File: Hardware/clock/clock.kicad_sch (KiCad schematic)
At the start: 19 parts, among them J1 Barrel_Jack_Switch, U1 WEMOS_C3_mini, U2 MAX7221xNG, U3 SBC18-11EGWA, U4 LM2596S-5, U5 SBC18-11EGWA, U6 SBC18-11EGWA, U7 SBC18-11EGWA

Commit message: Refactor code structure for improved readability and maintainability
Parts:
- removed C3: 104, Capacitor_THT:C_Disc_D3.0mm_W1.6mm_P2.50mm, symbol SparkFun-Capacitor:C
- removed D1: M7, PCM_JLCPCB:D_SMA, symbol PCM_JLCPCB-Diodes:General,M7
- removed R1: 10k, Resistor_THT:R_Axial_DIN0204_L3.6mm_D1.6mm_P5.08mm_Horizontal, symbol Device:R
- removed U1: WEMOS_C3_mini, RF_Module:WEMOS_C3_mini, symbol RF_Module:WEMOS_C3_mini
- added C1: 10uF, Capacitor_SMD:CP_Elec_4x5.4, symbol SparkFun-Capacitor:C
- added C10, C11, C12, C2, C6, C8: 100nF, SparkFun-Capacitor:C_0805_2012Metric, symbol SparkFun-Capacitor:C
- added C7: 22uF, Capacitor_SMD:C_0805_2012Metric_Pad1.18x1.45mm_HandSolder, symbol SparkFun-Capacitor:C
- added D3: SS34, Diode_SMD:D_SMA, symbol Diode:SS34
- added J2: Conn_02x03_Top_Bottom, Connector_IDC:IDC-Header_2x03_P2.54mm_Horizontal, symbol Connector_Generic:Conn_02x03_Top_Bottom
- added Q1, Q2: BC817, Package_TO_SOT_SMD:SOT-23, symbol Transistor_BJT:BC817
- added R1, R2, R3, R4: 10kΩ, PCM_JLCPCB:R_0805, symbol PCM_JLCPCB-Resistors:0805,10kΩ
- added SW1: PTH_RA_h7.5mm, SparkFun-Switch:Push_PTH_RA_8-020_h7.5mm, symbol SparkFun-Switch:SPST_Push_PTH_RA_h7.5mm
- added U4: ESP32-WROOM-32, RF_Module:ESP32-WROOM-32, symbol RF_Module:ESP32-WROOM-32
- added U7: AMS1117-3.3, Package_TO_SOT_SMD:SOT-223-3_TabPin2, symbol Regulator_Linear:AMS1117-3.3
- C3: renamed from C1; footprint Capacitor_THT:C_Radial_D8.0mm_H11.5mm_P3.50mm -> Capacitor_THT:C_Radial_D6.3mm_H7.0mm_P2.50mm
- C4: value 1uF -> 100nF; footprint Capacitor_THT:C_Radial_D4.0mm_H5.0mm_P1.50mm -> SparkFun-Capacitor:C_0805_2012Metric
- C5: value 104 -> 22uF; footprint Capacitor_THT:C_Disc_D3.0mm_W1.6mm_P2.50mm -> SparkFun-Fuse:1206
- D1: renamed from D3; footprint SparkFun-LED:LED_0603_1608Metric_Red -> LED_THT:LED_D3.0mm
- D2: renamed from D4; footprint SparkFun-LED:LED_0603_1608Metric_Red -> LED_THT:LED_D3.0mm
- renumbered C2 to C9, D2 to D4, U3 to U1, U5 to U2, U6 to U3, U7 to U5, U2 to U6, U4 to U8
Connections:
- net +5V: now also C1.1, C10.1, C12.1, C2.1, J2.3 (Pin_3), R1.2, U7.3 (VI); no longer C4.1, C5.1
- net GND: now also C1.2, C10.2, C11.2, C12.2, C2.2, C6.2, C7.2, C8.2, J2.6 (Pin_6), SW1.1, U4.1 (GND), U4.15 (GND), U4.38 (GND), U4.39 (GND), U7.1 (GND)
- net pwr_in: now also C4.1, D3.1 (K)
- net at J1.1: now also D3.2 (A)
- net at U6.18 (ISET): now also R1.1
- net MOSI: now reaches U6.1 (DIN)
- net MOSI: now also U4.37 (IO23)
- net CS: now reaches U6.12 (~{CS})
- net CS: now also U4.29 (IO5)
- net CLK: now reaches U6.13 (CLK)
- net CLK: now also U4.30 (IO18)
- new net: Q1.1 (B), R3.2
- new net: Q2.1 (B), R2.2
- new net 3.3V: C5.1, C6.1, C7.1, C8.1, R4.2, U4.2 (VDD), U7.2 (VO)
- new net DTR: J2.1 (Pin_1), Q2.2 (E), R3.1
- new net EN: C11.1, Q1.3 (C), R4.1, SW1.2, U4.3 (EN)
- new net IO0: Q2.3 (C), U4.25 (IO0)
- new net RTS: J2.4 (Pin_4), Q1.2 (E), R2.1
- new net RXD0: J2.2 (Pin_2), U4.34 (RXD0/IO3)
- new net TXD0: J2.5 (Pin_5), U4.35 (TXD0/IO1)
- no-connect marks 0 -> 8
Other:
- moved on the sheet: C3, C9, D4, J1, L1, U8

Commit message: Refactor code structure for improved readability and maintainability
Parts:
- removed J2: Conn_02x03_Top_Bottom, Connector_IDC:IDC-Header_2x03_P2.54mm_Horizontal, symbol Connector_Generic:Conn_02x03_Top_Bottom
- added J3: Conn_02x03_Odd_Even, Connector_IDC:IDC-Header_2x03_P2.54mm_Horizontal, symbol Connector_Generic:Conn_02x03_Odd_Even
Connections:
- net +5V: now also J3.5 (Pin_5)
- net DTR: now also J3.1 (Pin_1)
- net GND: now also J3.6 (Pin_6)
- net RTS: now also J3.2 (Pin_2)
- net RXD0: now also J3.3 (Pin_3)
- net TXD0: now also J3.4 (Pin_4)
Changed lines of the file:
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@@
 	(wire
 		(pts
+			(xy 101.6 138.43) (xy 107.95 138.43)
+		)
+		(stroke
+			(width 0)
+			(type default)
+		)
+	)
+	(wire
+		(pts
 			(xy 21.59 163.83) (xy 26.67 163.83)
 		)
@@
 	(wire
 		(pts
-			(xy 101.6 120.65) (xy 106.68 120.65)
-		)
-		(stroke
-			(width 0)
-			(type default)
-		)
-	)
-	(wire
-		(pts
 			(xy 22.86 114.3) (xy 27.94 114.3)
 		)
@@
 	(wire
 		(pts
-			(xy 118.11 83.82) (xy 123.19 83.82)
+			(xy 46.99 87.63) (xy 46.99 90.17)
 		)
 		(stroke
@@
 	(wire
 		(pts
-			(xy 46.99 87.63) (xy 46.99 90.17)
+			(xy 22.86 111.76) (xy 27.94 111.76)
 		)
 		(stroke
@@
 	(wire
 		(pts
-			(xy 22.86 111.76) (xy 27.94 111.76)
+			(xy 116.84 86.36) (xy 123.19 86.36)
 		)
 		(stroke
@@
 	(wire
 		(pts
-			(xy 273.05 146.05) (xy 273.05 149.86)
+			(xy 101.6 148.59) (xy 107.95 148.59)
 		)
 		(stroke
@@
 	(wire
 		(pts
-			(xy 101.6 148.59) (xy 106.68 148.59)
+			(xy 273.05 146.05) (xy 273.05 149.86)
 		)
 		(stroke
@@
 	(wire
 		(pts
-			(xy 118.11 81.28) (xy 123.19 81.28)
-		)
-		(stroke
-			(width 0)
-			(type default)
-		)
-	)
-	(wire
-		(pts
 			(xy 40.64 114.3) (xy 43.18 114.3)
 		)
@@
 	(wire
 		(pts
-			(xy 243.84 147.32) (xy 243.84 146.05)
+			(xy 116.84 81.28) (xy 123.19 81.28)
 		)
 		(stroke
@@
 	(wire
 		(pts
-			(xy 44.45 118.11) (xy 44.45 116.84)
+			(xy 243.84 147.32) (xy 243.84 146.05)
 		)
 		(stroke
@@
 	(wire
 		(pts
-			(xy 17.78 59.69) (xy 20.32 59.69)
+			(xy 44.45 118.11) (xy 44.45 116.84)
 		)
 		(stroke
@@
 	(wire
 		(pts
-			(xy 143.51 60.96) (xy 147.32 60.96)
+			(xy 17.78 59.69) (xy 20.32 59.69)
 		)
 		(stroke
@@
 	(wire
 		(pts
-			(xy 255.27 146.05) (xy 261.62 146.05)
+			(xy 143.51 60.96) (xy 147.32 60.96)
 		)
 		(stroke
@@
 	(wire
 		(pts
-			(xy 57.15 96.52) (xy 57.15 99.06)
+			(xy 255.27 146.05) (xy 261.62 146.05)
 		)
 		(stroke
@@
 	(wire
 		(pts
-			(xy 118.11 86.36) (xy 123.19 86.36)
+			(xy 57.15 96.52) (xy 57.15 99.06)
 		)
 		(stroke
@@
 	(wire
 		(pts
+			(xy 116.84 83.82) (xy 123.19 83.82)
+		)
+		(stroke
+			(width 0)
+			(type default)
+		)
+	)
+	(wire
+		(pts
 			(xy 53.34 176.53) (xy 53.34 180.34)
 		)
@@
 	(wire
 		(pts
-			(xy 41.91 46.99) (xy 44.45 46.99)
+			(xy 101.6 120.65) (xy 106.68 120.65)
 		)
 		(stroke
@@
 	(wire
 		(pts
-			(xy 180.34 106.68) (xy 180.34 110.49)
+			(xy 41.91 46.99) (xy 44.45 46.99)
 		)
 		(stroke
@@
 	(wire
 		(pts
-			(xy 38.1 171.45) (xy 45.72 171.45)
+			(xy 180.34 106.68) (xy 180.34 110.49)
 		)
 		(stroke
@@
 	(wire
 		(pts
-			(xy 101.6 138.43) (xy 106.68 138.43)
+			(xy 38.1 171.45) (xy 45.72 171.45)
 		)
 		(stroke
@@
 		)
 	)
-	(label "MOSI"
-		(at 118.11 86.36 0)
+	(label "CS"
+		(at 116.84 81.28 0)
 		(effects
 			(font
@@
 		)
 	)
-	(label "CLK"
-		(at 106.68 138.43 0)
-		(effects
-			(font
-				(size 1.27 1.27)
-			)
-			(justify left bottom)
-		)
-	)
 	(label "D"
 		(at 147.32 53.34 0)
@@
 		)
 	)
-	(label "CS"
-		(at 118.11 81.28 0)
-		(effects
-			(font
-				(size 1.27 1.27)
-			)
-			(justify left bottom)
-		)
-	)
 	(label "TXD0"
 		(at 43.18 114.3 0)
@@
 		)
 	)
-	(label "MOSI"
-		(at 106.68 148.59 0)
-		(effects
-			(font
-				(size 1.27 1.27)
-			)
-			(justify left bottom)
-		)
-	)
 	(label "A"
 		(at 147.32 45.72 0)
@@
 		)
 	)
-	(label "CS"
-		(at 106.68 120.65 0)
+	(label "G"
+		(at 83.82 62.23 0)
 		(effects
 			(font
@@
 		)
 	)
-	(label "G"
-		(at 83.82 62.23 0)
+	(label "CLK"
+		(at 107.95 138.43 0)
 		(effects
 			(font
@@
 		)
 	)
-	(label "CLK"
-		(at 118.11 83.82 0)
-		(effects
-			(font
-				(size 1.27 1.27)
-			)
-			(justify left bottom)
-		)
-	)
 	(label "pwr_in"
 		(at 200.66 137.16 0)
@@
 		)
 	)
+	(label "CS"
+		(at 106.68 120.65 0)
+		(effects
+			(font
+				(size 1.27 1.27)
+			)
+			(justify left bottom)
+		)
+	)
+	(label "MOSI"
+		(at 116.84 86.36 0)
+		(effects
+			(font
+				(size 1.27 1.27)
+			)
+			(justify left bottom)
+		)
+	)
 	(label "C"
 		(at 17.78 52.07 0)
@@
 		)
 	)
+	(label "CLK"
+		(at 116.84 83.82 0)
+		(effects
+			(font
+				(size 1.27 1.27)
+			)
+			(justify left bottom)
+		)
+	)
 	(label "B"
 		(at 41.91 49.53 0)
@@
 		)
 	)
+	(label "MOSI"
+		(at 107.95 148.59 0)
+		(effects
+			(font
+				(size 1.27 1.27)
+			)
+			(justify left bottom)
+		)
+	)
 	(label "DTR"
 		(at 22.86 111.76 0)
@@
 	)
 	(symbol
+		(lib_id "Connector_Generic:Conn_02x03_Odd_Even")
+		(at 33.02 114.3 0)
+		(unit 1)
+		(exclude_from_sim no)
+		(in_bom yes)
+		(on_board yes)
+		(dnp no)
+		(fields_autoplaced yes)
+		(property "Reference" "J3"
+			(at 34.29 105.41 0)
+			(effects
+				(font
+					(size 1.27 1.27)
+				)
+			)
+		)
+		(property "Value" "Conn_02x03_Odd_Even"
+			(at 34.29 107.95 0)
+			(effects
+				(font
+					(size 1.27 1.27)
+				)
+			)
+		)
+		(property "Footprint" "Connector_IDC:IDC-Header_2x03_P2.54mm_Horizontal"
+			(at 33.02 114.3 0)
+			(effects
+				(font
+					(size 1.27 1.27)
+				)
+				(hide yes)
+			)
+		)
+		(property "Datasheet" "~"
+			(at 33.02 114.3 0)
+			(effects
+				(font
+					(size 1.27 1.27)
+				)
+				(hide yes)
+			)
+		)
+		(property "Description" "Generic connector, double row, 02x03, odd/even pin numbering scheme (row 1 odd numbers, row 2 even numbers), script generated (kicad-library-utils/schlib/autogen/connector/)"
+			(at 33.02 114.3 0)
+			(effects
+				(font
+					(size 1.27 1.27)
+				)
+				(hide yes)
+			)
+		)
+		(pin "1"
+		)
+		(pin "4"
+		)
+		(pin "3"
+		)
+		(pin "5"
+		)
+		(pin "2"
+		)
+		(pin "6"
+		)
+		(instances
+			(project ""
+				(path "/1ff2a468-a5e0-4316-b62a-bd1e9ae7f68a"
+					(reference "J3")
+					(unit 1)
+				)
+			)
+		)
+	)
+	(symbol
 		(lib_id "power:GND")
 		(at 214.63 119.38 0)
@@
 					(unit 1)
 				)
-			)
-		)
-	)
-	(symbol
-		(lib_id "Connector_Generic:Conn_02x03_Top_Bottom")
-		(at 33.02 114.3 0)
-		(unit 1)
-		(exclude_from_sim no)
-		(in_bom yes)
-		(on_board yes)
-		(dnp no)
-		(fields_autoplaced yes)
-		(property "Reference" "J2"
-			(at 34.29 105.41 0)
-			(effects
-				(font
-					(size 1.27 1.27)
-				)
-			)
-		)
-		(property "Value" "Conn_02x03_Top_Bottom"
-			(at 34.29 107.95 0)
-			(effects
-				(font
-					(size 1.27 1.27)
-				)
-			)
-		)
-		(property "Footprint" "Connector_IDC:IDC-Header_2x03_P2.54mm_Horizontal"
-			(at 33.02 114.3 0)
-			(effects
-				(font
-					(size 1.27 1.27)
-				)
-				(hide yes)
-			)
-		)
-		(property "Datasheet" "~"
-			(at 33.02 114.3 0)
-			(effects
-				(font
-					(size 1.27 1.27)
-				)
-				(hide yes)
-			)
-		)
-		(property "Description" "Generic connector, double row, 02x03, top/bottom pin numbering scheme (row 1: 1...pins_per_row, row2: pins_per_row+1 ... num_pins), script generated (kicad-library-utils/schlib/autogen/connector/)"
-			(at 33.02 114.3 0)
-			(effects
-				(font
-					(size 1.27 1.27)
-				)
-				(hide yes)
-			)
-		)
-		(pin "4"
-		)
-		(pin "6"
-		)
-		(pin "1"
-		)
-		(pin "2"
-		)
-		(pin "3"
-		)
-		(pin "5"
-		)
-		(instances
-			(project ""
-				(path "/1ff2a468-a5e0-4316-b62a-bd1e9ae7f68a"
-					(reference "J2")
-					(unit 1)
-				)

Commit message: Updated README.md
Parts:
- added D5: LED, SparkFun-LED:LED_0603_1608Metric, symbol SparkFun-LED:LED
- added J2: Conn_01x05_Pin, Connector_PinHeader_2.54mm:PinHeader_1x05_P2.54mm_Vertical, symbol Connector:Conn_01x05_Pin
- added J4: Conn_01x02_Pin, Connector_PinHeader_2.00mm:PinHeader_1x02_P2.00mm_Vertical, symbol Connector:Conn_01x02_Pin
- added R5: 1.5k, SparkFun-Resistor:R_0603_1608Metric, symbol SparkFun-Resistor:1.5k_0603
- added R6, R7: 4.7k, SparkFun-Resistor:R_0603_1608Metric, symbol SparkFun-Resistor:4.7k_0603
- J3: footprint Connector_IDC:IDC-Header_2x03_P2.54mm_Horizontal -> Connector_PinHeader_2.54mm:PinHeader_1x06_P2.54mm_Vertical
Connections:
- net 3.3V: now also R6.2, R7.2
- net GND: now also J2.5 (Pin_5), R5.2
- net 14: now reaches U4.13 (IO14)
- net 12: now reaches U4.14 (IO12)
- net 13: now reaches U4.16 (IO13)
- net 15: now reaches U4.23 (IO15)
- net 2: now reaches U4.24 (IO2)
- net 2: now also D5.1 (K)
- net 16: now reaches U4.27 (IO16)
- net SDA: now reaches U4.33 (IO21)
- net SDA: now also J4.1 (Pin_1), R6.1
- net SCL: now reaches U4.36 (IO22)
- net SCL: now also J4.2 (Pin_2), R7.1
- net ADC_3: now reaches U4.6 (IO34)
- net ADC_3: now also J2.3 (Pin_3)
- net ADC_4: now reaches U4.7 (IO35)
- net ADC_4: now also J2.4 (Pin_4)
- net ADC_1: now reaches U4.8 (IO32)
- net ADC_1: now also J2.1 (Pin_1)
- net ADC_2: now reaches U4.9 (IO33)
- net ADC_2: now also J2.2 (Pin_2)
- new net: D5.2 (A), R5.1
- no-connect marks 8 -> 14
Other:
- moved on the sheet: C1, C10, C11, C12, C2, C3, C4, C5, C6, C7, C8, C9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

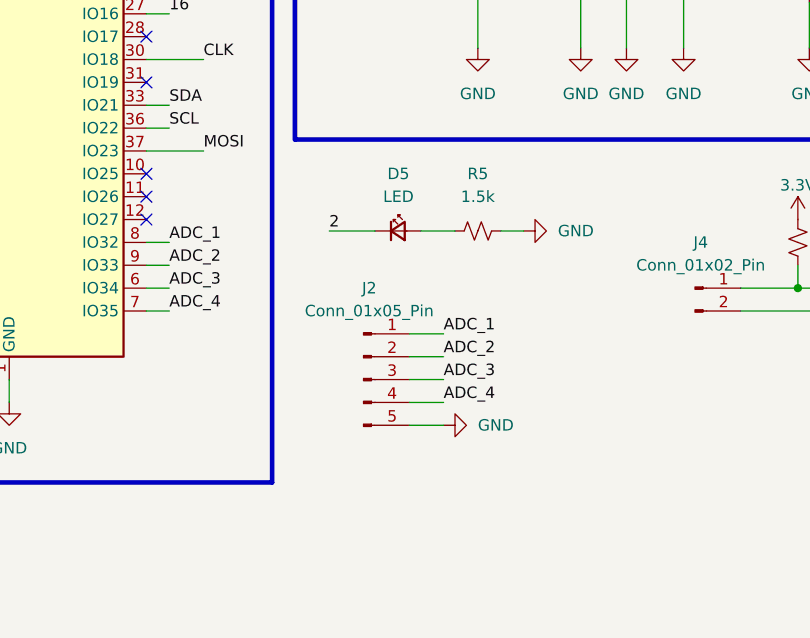
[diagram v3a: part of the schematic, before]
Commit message: Add initial PCB lock file and component list for clock project
- Created a lock file for the PCB design with hostname and username.
- Added a comprehensive CSV file listing components for the clock project, including values, footprints, and datasheets for each component.
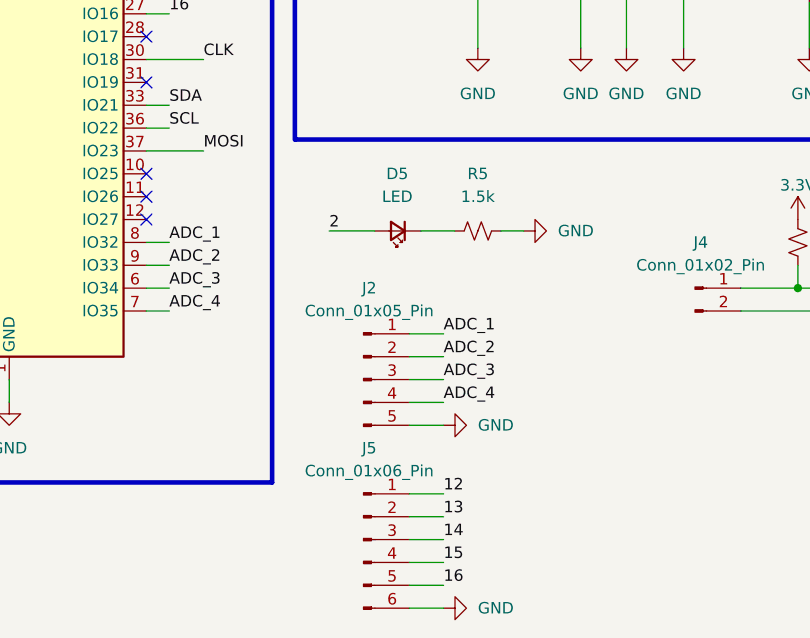
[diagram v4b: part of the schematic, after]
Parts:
- added J5: Conn_01x06_Pin, Connector_PinSocket_2.54mm:PinSocket_1x06_P2.54mm_Vertical, symbol Connector:Conn_01x06_Pin
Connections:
- net 12: now also J5.1 (Pin_1)
- net 13: now also J5.2 (Pin_2)
- net 14: now also J5.3 (Pin_3)
- net 15: now also J5.4 (Pin_4)
- net 16: now also J5.5 (Pin_5)
- net 2: now also D5.2 (A); no longer D5.1 (K)
- net GND: now also J5.6 (Pin_6)
- net at R5.1: now also D5.1 (K); no longer D5.2 (A)
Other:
- moved on the sheet: D5
